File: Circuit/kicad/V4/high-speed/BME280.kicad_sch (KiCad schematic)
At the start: 2 parts, among them U56 BME280

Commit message: high speed first step
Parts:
- renumbered C107 to C44, U56 to U21
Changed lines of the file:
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@@
 		(on_board yes)
 		(dnp no)
-		(property "Reference" "#PWR0150"
+		(property "Reference" "#PWR0140"
 			(at 113.03 73.66 0)
 			(effects
@@
 		)
 		(instances
-			(project "CM5IO"
-				(path "/e63e39d7-6ac0-4ffd-8aa3-1841a4541b55/a83afe30-5c7e-43cb-a5b2-f6f97a0812b3/86209e6a-92ae-4699-a125-02d46b525fc7/160ccd78-386a-4b8b-89f3-6c9a73a758a1"
-					(reference "#PWR0150")
+			(project "high-speed"
+				(path "/e63e39d7-6ac0-4ffd-8aa3-1841a4541b55/a83afe30-5c7e-43cb-a5b2-f6f97a0812b3/22db6783-000b-491c-a9a9-359609b9f1e7"
+					(reference "#PWR0140")
 					(unit 1)
 				)
@@
 		(on_board yes)
 		(dnp no)
-		(property "Reference" "#PWR0149"
+		(property "Reference" "#PWR0139"
 			(at 107.95 73.66 0)
 			(effects
@@
 		)
 		(instances
-			(project "CM5IO"
-				(path "/e63e39d7-6ac0-4ffd-8aa3-1841a4541b55/a83afe30-5c7e-43cb-a5b2-f6f97a0812b3/86209e6a-92ae-4699-a125-02d46b525fc7/160ccd78-386a-4b8b-89f3-6c9a73a758a1"
-					(reference "#PWR0149")
+			(project "high-speed"
+				(path "/e63e39d7-6ac0-4ffd-8aa3-1841a4541b55/a83afe30-5c7e-43cb-a5b2-f6f97a0812b3/22db6783-000b-491c-a9a9-359609b9f1e7"
+					(reference "#PWR0139")
 					(unit 1)
 				)
@@
 		(dnp no)
 		(fields_autoplaced yes)
-		(property "Reference" "U56"
+		(property "Reference" "U21"
 			(at 99.06 50.7999 0)
 			(effects
@@
 		)
 		(instances
-			(project ""
-				(path "/e63e39d7-6ac0-4ffd-8aa3-1841a4541b55/a83afe30-5c7e-43cb-a5b2-f6f97a0812b3/86209e6a-92ae-4699-a125-02d46b525fc7/160ccd78-386a-4b8b-89f3-6c9a73a758a1"
-					(reference "U56")
+			(project "high-speed"
+				(path "/e63e39d7-6ac0-4ffd-8aa3-1841a4541b55/a83afe30-5c7e-43cb-a5b2-f6f97a0812b3/22db6783-000b-491c-a9a9-359609b9f1e7"
+					(reference "U21")
 					(unit 1)
 				)
@@
 		(dnp no)
 		(fields_autoplaced yes)
-		(property "Reference" "C107"
+		(property "Reference" "C44"
 			(at 73.66 59.69 90)
 			(effects
@@
 		)
 		(instances
-			(project "CM5IO"
-				(path "/e63e39d7-6ac0-4ffd-8aa3-1841a4541b55/a83afe30-5c7e-43cb-a5b2-f6f97a0812b3/86209e6a-92ae-4699-a125-02d46b525fc7/160ccd78-386a-4b8b-89f3-6c9a73a758a1"
-					(reference "C107")
+			(project "high-speed"
+				(path "/e63e39d7-6ac0-4ffd-8aa3-1841a4541b55/a83afe30-5c7e-43cb-a5b2-f6f97a0812b3/22db6783-000b-491c-a9a9-359609b9f1e7"
+					(reference "C44")
 					(unit 1)
 				)
@@
 		(on_board yes)
 		(dnp no)
-		(property "Reference" "#PWR0148"
+		(property "Reference" "#PWR0138"
 			(at 83.82 67.31 0)
 			(effects
@@
 		)
 		(instances
-			(project "CM5IO"
-				(path "/e63e39d7-6ac0-4ffd-8aa3-1841a4541b55/a83afe30-5c7e-43cb-a5b2-f6f97a0812b3/86209e6a-92ae-4699-a125-02d46b525fc7/160ccd78-386a-4b8b-89f3-6c9a73a758a1"
-					(reference "#PWR0148")
-					(unit 1)
-				)
+			(project "high-speed"
+				(path "/e63e39d7-6ac0-4ffd-8aa3-1841a4541b55/a83afe30-5c7e-43cb-a5b2-f6f97a0812b3/22db6783-000b-491c-a9a9-359609b9f1e7"
+					(reference "#PWR0138")
+					(unit 1)
+				)

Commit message: kicad: high speed V2.2 Circuit finish psu bom update
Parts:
- removed C44: 1uf, Capacitor_SMD:C_0805_2012Metric, symbol Device:C
- added C39: 1uf, Capacitor_SMD:C_0805_2012Metric, symbol Device:C
- added C40: 100nf, Capacitor_SMD:C_0805_2012Metric, symbol Device:C
- added C41: 22nf c0g, Capacitor_SMD:C_0805_2012Metric, symbol Device:C
- U22: renamed from U21; Cikkszám (none) -> 100.490.91; Link (none) -> https://www.hestore.hu/prod_10049091.html
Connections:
- net 3V3: now also C39.1, C40.1, C41.1
- net GND: now also C39.2, C40.2, C41.2

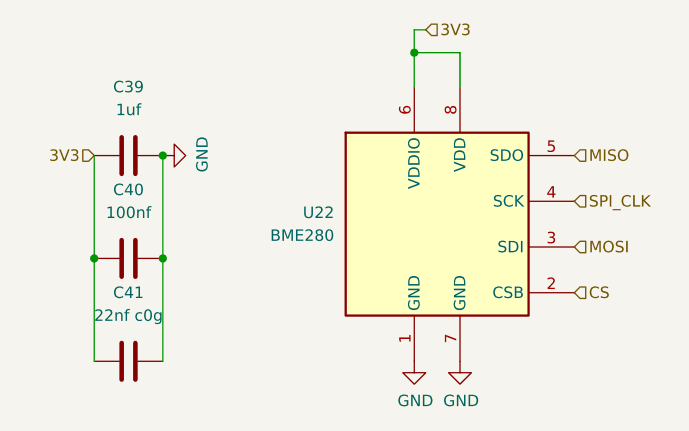
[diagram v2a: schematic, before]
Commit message: finished high-speed panel schematic and first try to doute gpios
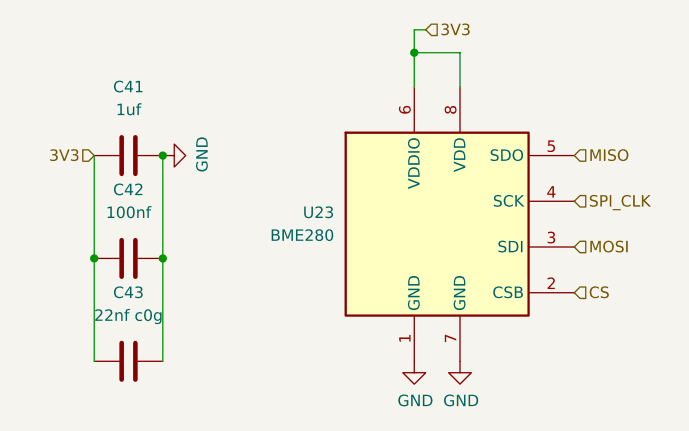
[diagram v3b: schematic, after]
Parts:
- renumbered C39 to C41, C40 to C42, C41 to C43, U22 to U23
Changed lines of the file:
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@@
 		(dnp no)
 		(fields_autoplaced yes)
-		(property "Reference" "C41"
+		(property "Reference" "C43"
 			(at 76.2 59.69 90)
 			(effects
@@
 			)
 		)
-		(property "Datasheet" "~"
+		(property "Datasheet" "https://www.hestore.hu/prod_getfile.php?id=3647"
 			(at 76.2 67.31 0)
 			(effects
@@
 		(instances
 			(project "high-speed"
-				(path "/e63e39d7-6ac0-4ffd-8aa3-1841a4541b55/a83afe30-5c7e-43cb-a5b2-f6f97a0812b3/22db6783-000b-491c-a9a9-359609b9f1e7"
-					(reference "C41")
+				(path "/e63e39d7-6ac0-4ffd-8aa3-1841a4541b55/e6a127e0-e8a4-4ccd-bbc7-ce5df0e2aadb/22db6783-000b-491c-a9a9-359609b9f1e7"
+					(reference "C43")
 					(unit 1)
 				)
@@
 		(on_board yes)
 		(dnp no)
-		(property "Reference" "#PWR0123"
+		(property "Reference" "#PWR0135"
 			(at 113.03 73.66 0)
 			(effects
@@
 		(instances
 			(project "high-speed"
-				(path "/e63e39d7-6ac0-4ffd-8aa3-1841a4541b55/a83afe30-5c7e-43cb-a5b2-f6f97a0812b3/22db6783-000b-491c-a9a9-359609b9f1e7"
-					(reference "#PWR0123")
+				(path "/e63e39d7-6ac0-4ffd-8aa3-1841a4541b55/e6a127e0-e8a4-4ccd-bbc7-ce5df0e2aadb/22db6783-000b-491c-a9a9-359609b9f1e7"
+					(reference "#PWR0135")
 					(unit 1)
 				)
@@
 		(on_board yes)
 		(dnp no)
-		(property "Reference" "#PWR0122"
+		(property "Reference" "#PWR0134"
 			(at 107.95 73.66 0)
 			(effects
@@
 		(instances
 			(project "high-speed"
-				(path "/e63e39d7-6ac0-4ffd-8aa3-1841a4541b55/a83afe30-5c7e-43cb-a5b2-f6f97a0812b3/22db6783-000b-491c-a9a9-359609b9f1e7"
-					(reference "#PWR0122")
+				(path "/e63e39d7-6ac0-4ffd-8aa3-1841a4541b55/e6a127e0-e8a4-4ccd-bbc7-ce5df0e2aadb/22db6783-000b-491c-a9a9-359609b9f1e7"
+					(reference "#PWR0134")
 					(unit 1)
 				)
@@
 		(dnp no)
 		(fields_autoplaced yes)
-		(property "Reference" "U22"
+		(property "Reference" "U23"
 			(at 99.06 50.7999 0)
 			(effects
@@
 			)
 		)
-		(property "Datasheet" "https://www.bosch-sensortec.com/media/boschsensortec/downloads/datasheets/bst-bme280-ds002.pdf"
+		(property "Datasheet" "https://www.hestore.hu/prod_getfile.php?id=20045"
 			(at 110.49 57.15 0)
 			(effects
@@
 		(instances
 			(project "high-speed"
-				(path "/e63e39d7-6ac0-4ffd-8aa3-1841a4541b55/a83afe30-5c7e-43cb-a5b2-f6f97a0812b3/22db6783-000b-491c-a9a9-359609b9f1e7"
-					(reference "U22")
+				(path "/e63e39d7-6ac0-4ffd-8aa3-1841a4541b55/e6a127e0-e8a4-4ccd-bbc7-ce5df0e2aadb/22db6783-000b-491c-a9a9-359609b9f1e7"
+					(reference "U23")
 					(unit 1)
 				)
@@
 		(dnp no)
 		(fields_autoplaced yes)
-		(property "Reference" "C40"
+		(property "Reference" "C42"
 			(at 76.2 48.26 90)
 			(effects
@@
 			)
 		)
-		(property "Datasheet" "~"
+		(property "Datasheet" "-"
 			(at 76.2 55.88 0)
 			(effects
@@
 		(instances
 			(project "high-speed"
-				(path "/e63e39d7-6ac0-4ffd-8aa3-1841a4541b55/a83afe30-5c7e-43cb-a5b2-f6f97a0812b3/22db6783-000b-491c-a9a9-359609b9f1e7"
-					(reference "C40")
+				(path "/e63e39d7-6ac0-4ffd-8aa3-1841a4541b55/e6a127e0-e8a4-4ccd-bbc7-ce5df0e2aadb/22db6783-000b-491c-a9a9-359609b9f1e7"
+					(reference "C42")
 					(unit 1)
 				)
@@
 		(dnp no)
 		(fields_autoplaced yes)
-		(property "Reference" "C39"
+		(property "Reference" "C41"
 			(at 76.2 36.83 90)
 			(effects
@@
 			)
 		)
-		(property "Datasheet" "~"
+		(property "Datasheet" "https://www.hestore.hu/prod_getfile.php?id=4317"
 			(at 76.2 44.45 0)
 			(effects
@@
 		(instances
 			(project "high-speed"
-				(path "/e63e39d7-6ac0-4ffd-8aa3-1841a4541b55/a83afe30-5c7e-43cb-a5b2-f6f97a0812b3/22db6783-000b-491c-a9a9-359609b9f1e7"
-					(reference "C39")
+				(path "/e63e39d7-6ac0-4ffd-8aa3-1841a4541b55/e6a127e0-e8a4-4ccd-bbc7-ce5df0e2aadb/22db6783-000b-491c-a9a9-359609b9f1e7"
+					(reference "C41")
 					(unit 1)
 				)
@@
 		(on_board yes)
 		(dnp no)
-		(property "Reference" "#PWR0121"
+		(property "Reference" "#PWR0133"
 			(at 86.36 44.45 0)
 			(effects
@@
 		(instances
 			(project "high-speed"
-				(path "/e63e39d7-6ac0-4ffd-8aa3-1841a4541b55/a83afe30-5c7e-43cb-a5b2-f6f97a0812b3/22db6783-000b-491c-a9a9-359609b9f1e7"
-					(reference "#PWR0121")
-					(unit 1)
-				)
+				(path "/e63e39d7-6ac0-4ffd-8aa3-1841a4541b55/e6a127e0-e8a4-4ccd-bbc7-ce5df0e2aadb/22db6783-000b-491c-a9a9-359609b9f1e7"
+					(reference "#PWR0133")
+					(unit 1)
+				)
